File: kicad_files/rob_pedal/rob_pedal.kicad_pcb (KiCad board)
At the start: 2 copper layers, 52 parts, among them J1 OD_IN, J2 ODR_OUT, J3 9V, J4 SHO_IN, J5 SHO_OUT, Q1 BS170, Q2 BS170, Q3 BS170, Q4 BS170

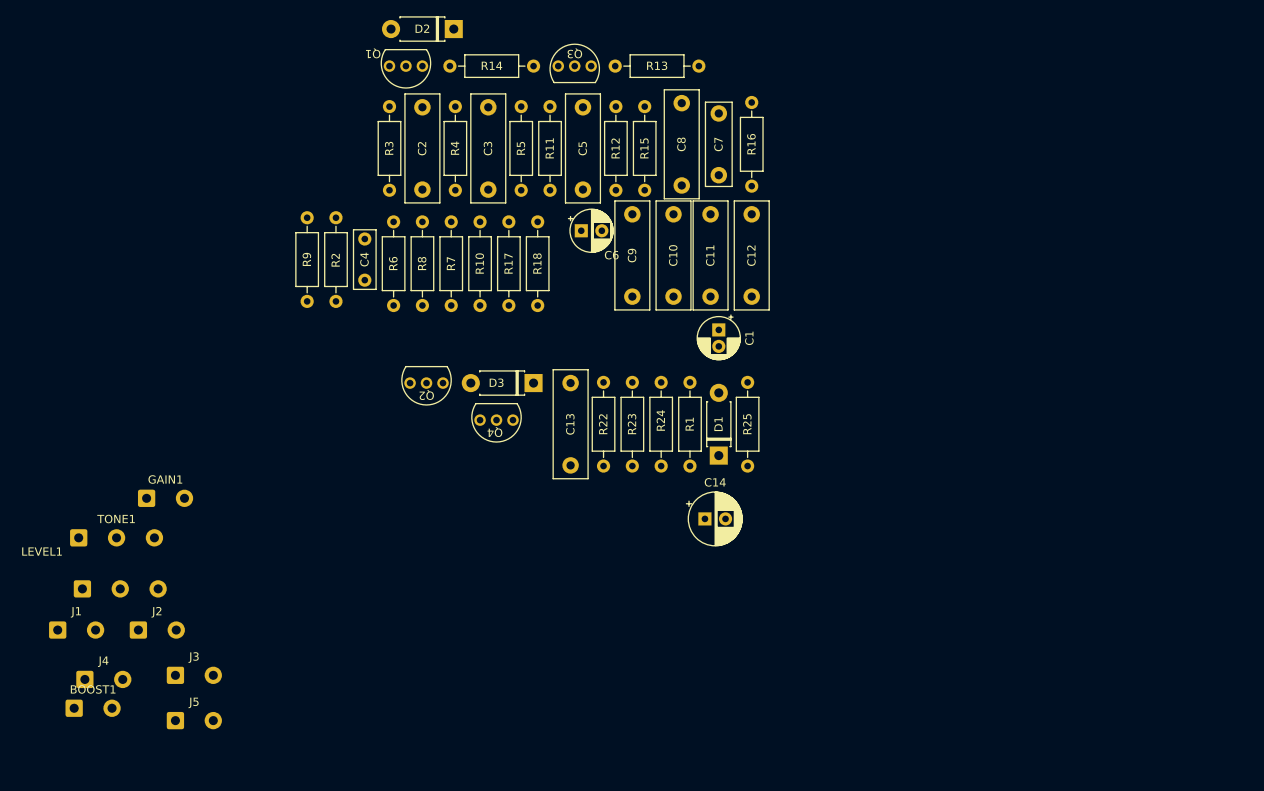
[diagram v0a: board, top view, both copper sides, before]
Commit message: first placement for 125B case
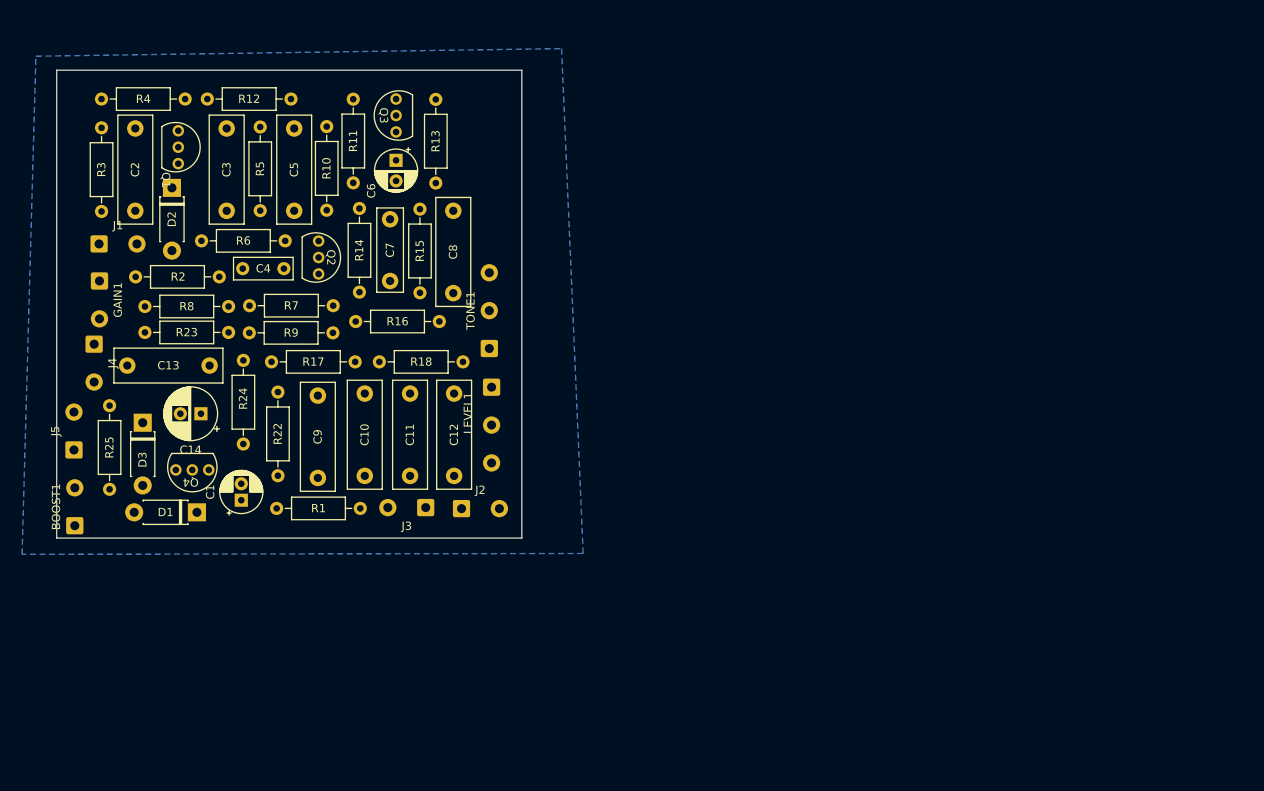
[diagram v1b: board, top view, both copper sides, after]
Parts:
- moved R25 77.8 mm to (52.0, 73.7), turned to -90 degrees
- moved D1 63.8 mm to (62.6, 86.7), turned to 180 degrees
- moved C14 62.5 mm to (63.1, 74.7), turned to 180 degrees
- moved C1 61.6 mm to (68.0, 85.2), turned to 90 degrees
- moved LEVEL1 55.4 mm to (98.4, 71.5), turned to -90 degrees
- moved C13 55.2 mm to (54.1, 68.9), turned to 0 degrees
- moved R16 55.0 mm to (81.9, 63.5), turned to 0 degrees
- moved TONE1 54.9 mm to (98.1, 66.8), turned to 90 degrees
- moved R23 51.7 mm to (66.5, 64.8), turned to 180 degrees
- moved R12 50.8 mm to (63.9, 36.5), turned to 0 degrees
- moved R24 50.8 mm to (68.2, 78.4)
- moved C11 48.4 mm to (88.5, 82.3), turned to 90 degrees
- moved C12 48.1 mm to (93.8, 82.3), turned to 90 degrees
- moved D3 47.7 mm to (56.0, 75.8), turned to -90 degrees
- moved J1 47.2 mm to (50.7, 54.1)
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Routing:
- added copper zone on B.Cu, net GND
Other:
- board outline added: 56.5 x 56.8 mm

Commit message: added routing
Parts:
- moved C1 116.4 mm to (184.3, 79.5), turned to 180 degrees
- moved R8 114.5 mm to (167.8, 87.7), turned to -90 degrees
- moved D1 111.5 mm to (170.5, 115.0), turned to 0 degrees
- moved R7 102.2 mm to (164.5, 97.8), turned to 90 degrees
- moved J5 100.0 mm to (141.0, 115.0), turned to 0 degrees
- moved R14 99.0 mm to (174.8, 85.2), turned to 90 degrees
- moved R18 98.4 mm to (173.3, 111.3), turned to 90 degrees
- moved R25 97.4 mm to (142.4, 110.0), turned to 180 degrees
- moved R9 97.0 mm to (154.0, 111.6), turned to 90 degrees
- moved C7 96.1 mm to (174.5, 88.8)
- moved R15 96.0 mm to (178.0, 87.4)
- moved C8 95.9 mm to (182.0, 97.5)
- moved R16 95.5 mm to (171.0, 97.8), turned to 90 degrees
- moved R24 95.0 mm to (157.3, 111.6)
- moved R17 94.8 mm to (160.5, 101.4), turned to -90 degrees
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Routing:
- net VCC: track 0.00 -> 134.8 mm
- net Net-(C14-Pad1): track 0.00 -> 32.3 mm
- net Net-(D2-Pad2): track 0.00 -> 29.8 mm
- net Net-(R17-Pad1): track 0.00 -> 29.4 mm
- net Net-(BOOST1-Pad1): track 0.00 -> 27.6 mm
- net Net-(C13-Pad2): track 0.00 -> 25.8 mm
- net ODR_IN: track 0.00 -> 21.3 mm
- net Net-(C2-Pad2): track 0.00 -> 20.8 mm
- net Net-(C7-Pad2): track 0.00 -> 19.4 mm
- net Net-(C6-Pad1): track 0.00 -> 19.1 mm
- net Net-(C4-Pad2): track 0.00 -> 18.8 mm
- net IN3: track 0.00 -> 16.3 mm
- net 9V: track 0.00 -> 13.3 mm
- net Net-(C3-Pad1): track 0.00 -> 13.3 mm
- net Net-(C11-Pad2): track 0.00 -> 13.2 mm
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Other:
- board size 56.5 x 56.8 mm -> 63.5 x 46.8 mm

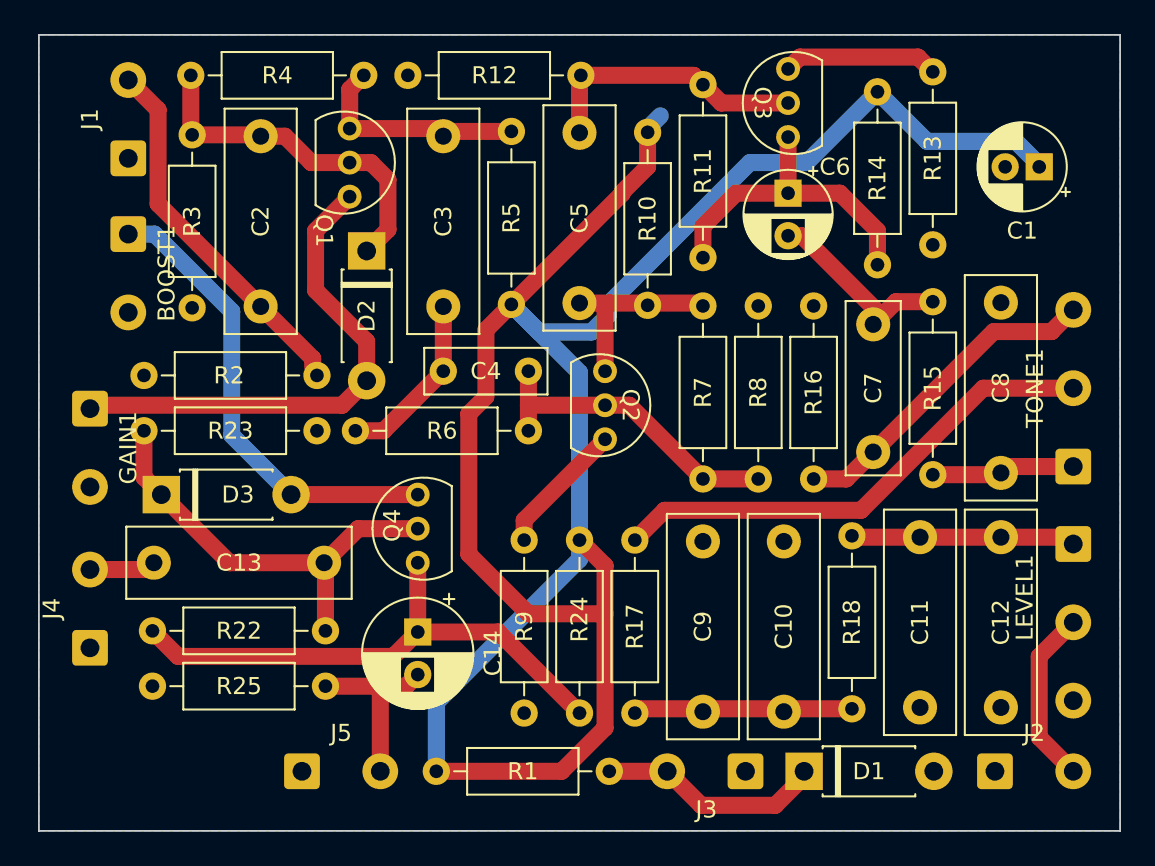
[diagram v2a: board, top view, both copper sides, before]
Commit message: added mounting holes
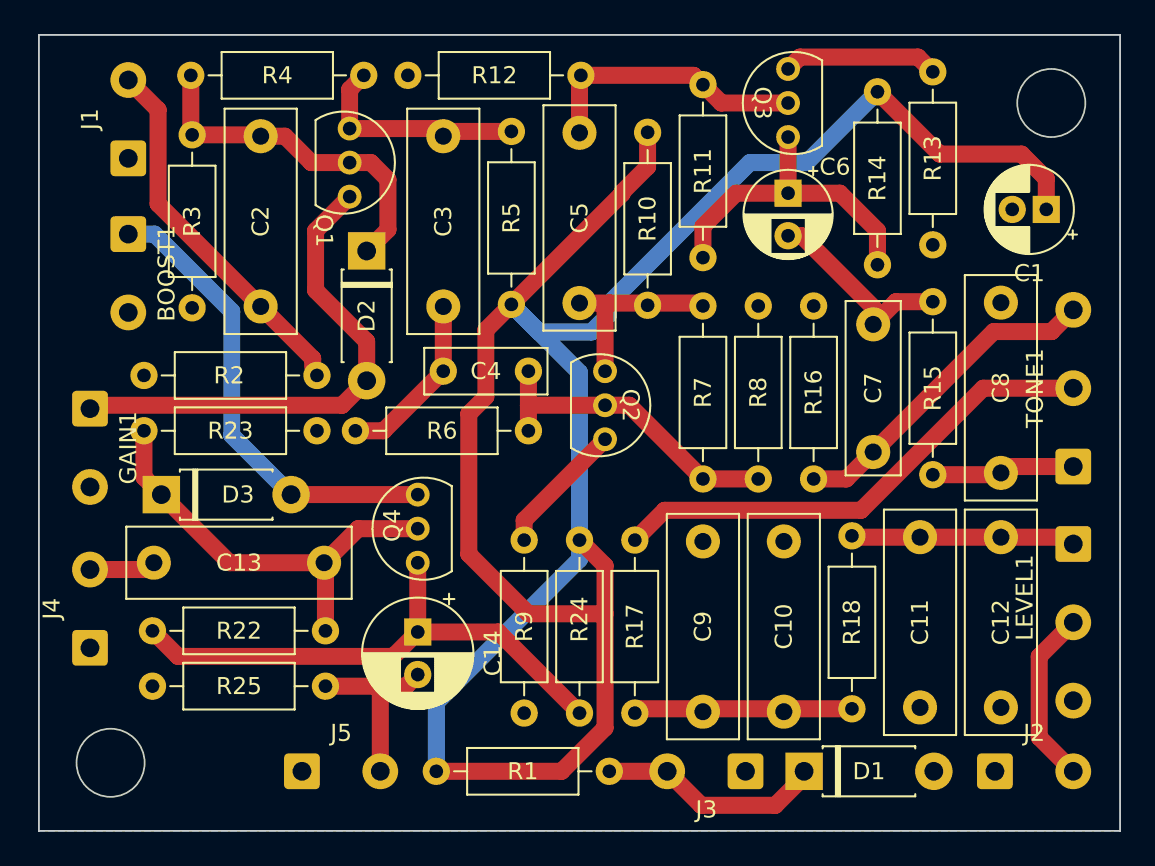
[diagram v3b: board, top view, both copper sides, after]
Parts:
- moved C1 2.53 mm to (184.7, 82.0)
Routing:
- net VCC: track 134.8 -> 136.2 mm
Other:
- outline, holes or cut-outs redrawn
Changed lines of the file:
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@@
   )
   (footprint "Capacitor_THT:CP_Radial_D5.0mm_P2.00mm" (layer "F.Cu")
-    (at 184.29 79.5 180)
+    (at 184.705113 82 180)
     (descr "CP, Radial series, Radial, pin pitch=2.00mm, , diameter=5mm, Electrolytic Capacitor")
     (tags "CP Radial series Radial pin pitch 2.00mm  diameter 5mm Electrolytic Capacitor")
@@
       (net 21 "Net-(D2-Pad2)") (pinfunction "S") (pintype "passive"))
   )
+  (gr_circle (center 129.75 114.5) (end 131.75 114.5) (layer "Edge.Cuts") (width 0.1) (fill none))
   (gr_rect (start 125.54 71.75) (end 189.04 118.5) (layer "Edge.Cuts") (width 0.1) (fill none))
+  (gr_circle (center 185 75.75) (end 187 75.75) (layer "Edge.Cuts") (width 0.1) (fill none))
   (gr_circle (center 123.75 54.496095) (end 131.75 54.246095) (layer "User.1") (width 0.15) (fill none))
   (gr_rect (start 110 39.25) (end 204 158.25) (layer "User.1") (width 0.15) (fill none))
@@
   (segment (start 156.241608 115) (end 158.79 112.451608) (width 1) (layer "F.Cu") (net 3))
   (segment (start 154.29 105.75) (end 150.79 102.25) (width 1) (layer "F.Cu") (net 3))
+  (segment (start 178.45 78.75) (end 183.255113 78.75) (width 1) (layer "F.Cu") (net 3))
   (segment (start 158.79 102.92) (end 157.29 101.42) (width 1) (layer "F.Cu") (net 3))
   (segment (start 159.79 81.08) (end 159.79 81) (width 1) (layer "F.Cu") (net 3))
+  (segment (start 174.79 75.09) (end 178.45 78.75) (width 1) (layer "F.Cu") (net 3))
+  (segment (start 184.705113 80.2) (end 184.705113 82) (width 1) (layer "F.Cu") (net 3))
   (segment (start 159.79 81) (end 161.29 79.5) (width 1) (layer "F.Cu") (net 3))
   (segment (start 150.79 94) (end 151.79 93) (width 1) (layer "F.Cu") (net 3))
@@
   (segment (start 161.29 79.5) (end 161.29 77.47) (width 1) (layer "F.Cu") (net 3))
   (segment (start 148.88 115) (end 156.241608 115) (width 1) (layer "F.Cu") (net 3))
+  (segment (start 183.255113 78.75) (end 184.705113 80.2) (width 1) (layer "F.Cu") (net 3))
   (segment (start 157.29 101.42) (end 157.29 91.58) (width 1) (layer "B.Cu") (net 3))
   (segment (start 153.29 87.58) (end 154.909511 89.199511) (width 1) (layer "B.Cu") (net 3))
   (segment (start 161.29 77.47) (end 161.29 77.25) (width 1) (layer "B.Cu") (net 3))
   (segment (start 157.29 102.55137) (end 148.88 110.96137) (width 1) (layer "B.Cu") (net 3))
-  (segment (start 184.29 79.37937) (end 182.911119 78.000489) (width 1) (layer "B.Cu") (net 3))
   (segment (start 157.29 101.42) (end 157.29 102.55137) (width 1) (layer "B.Cu") (net 3))
   (segment (start 158.989511 87.550489) (end 167.29 79.25) (width 1) (layer "B.Cu") (net 3))
-  (segment (start 182.911119 78.000489) (end 177.700489 78.000489) (width 1) (layer "B.Cu") (net 3))
   (segment (start 157.993962 89.199511) (end 158.989511 88.203962) (width 1) (layer "B.Cu") (net 3))
   (segment (start 158.989511 88.203962) (end 158.989511 87.550489) (width 1) (layer "B.Cu") (net 3))
   (segment (start 170.63 79.25) (end 174.79 75.09) (width 1) (layer "B.Cu") (net 3))
-  (segment (start 184.29 79.5) (end 184.29 79.37937) (width 1) (layer "B.Cu") (net 3))
   (segment (start 148.88 110.96137) (end 148.88 115) (width 1) (layer "B.Cu") (net 3))
-  (segment (start 161.29 77.25) (end 162.04 76.5) (width 1) (layer "B.Cu") (net 3))
   (segment (start 154.909511 89.199511) (end 157.993962 89.199511) (width 1) (layer "B.Cu") (net 3))
-  (segment (start 177.700489 78.000489) (end 174.79 75.09) (width 1) (layer "B.Cu") (net 3))
   (segment (start 167.29 79.25) (end 170.63 79.25) (width 1) (layer "B.Cu") (net 3))
   (segment (start 157.29 91.58) (end 153.29 87.58) (width 1) (layer "B.Cu") (net 3))

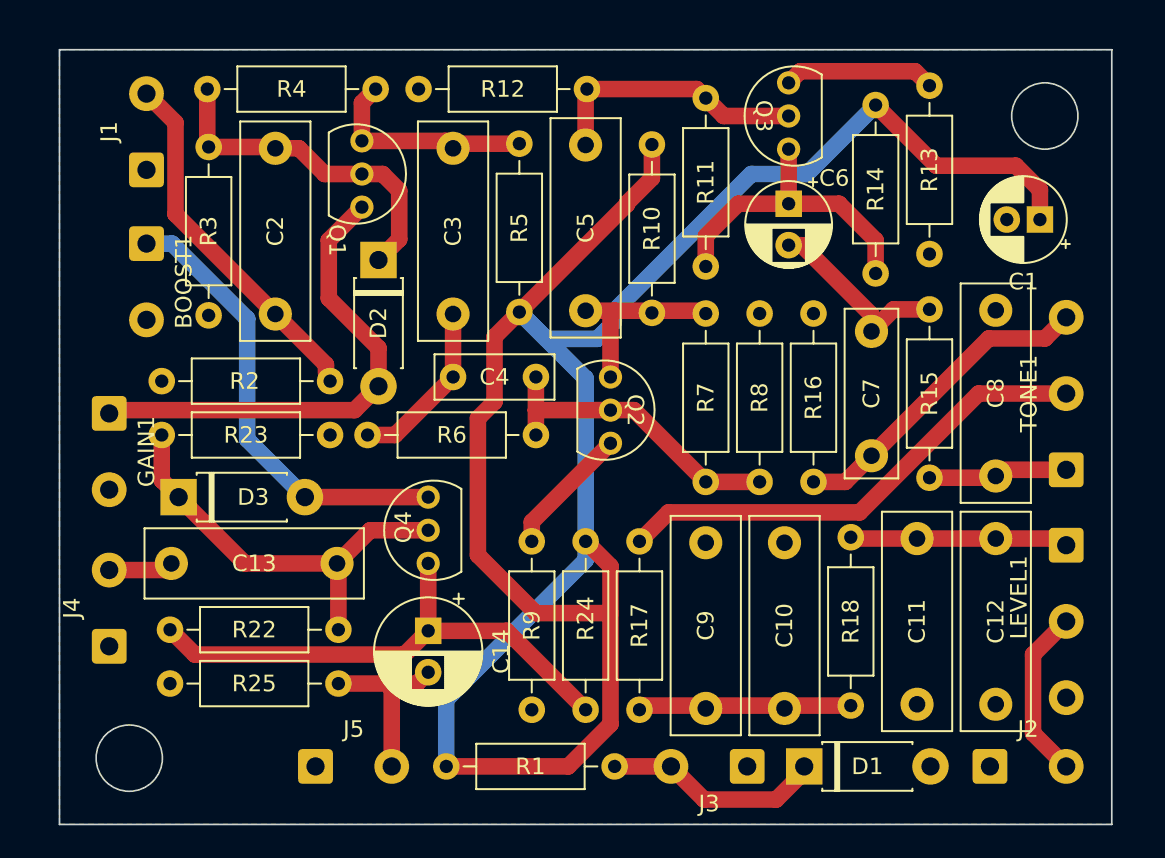
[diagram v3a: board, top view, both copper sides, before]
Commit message: added silkscreen and logo
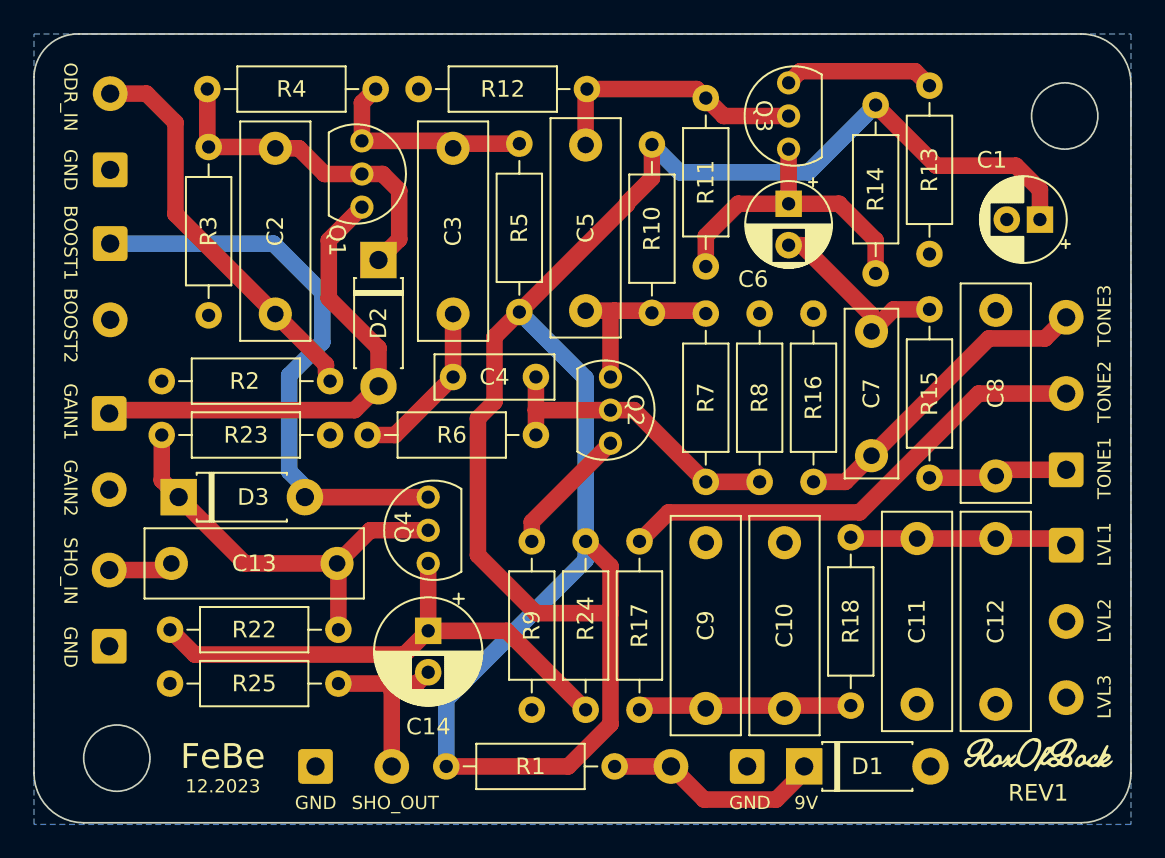
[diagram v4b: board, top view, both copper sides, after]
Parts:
- removed J2: ODR_OUT, Connector_Wire:SolderWire-0.5sqmm_1x02_P4.6mm_D0.9mm_OD2.1mm
- added REV1: logo, footprints:logo, F.Cu at (184.6, 119.3)
- moved BOOST1 2.19 mm to (128.6, 83.5)
- moved J1 2.19 mm to (128.6, 79.0)
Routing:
- net VCC: track 136.2 -> 123.7 mm
- net ODR_OUT: track 10.4 -> 0.00 mm
- net Net-(BOOST1-Pad1): track 27.6 -> 35.0 mm
- net ODR_IN: track 21.3 -> 23.5 mm
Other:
- board size 63.5 x 46.8 mm -> 66.2 x 47.6 mm
- board text added: "12.2023"
- board text added: "9V"
- board text added: "BOOST1"
- board text added: "BOOST2"
- board text added: "FeBe"
- board text added: "GAIN1"
- board text added: "GAIN2"
- board text added: "GND"
- board text added: "LVL1"
- board text added: "LVL2"
- board text added: "LVL3"
- board text added: "ODR_IN"
- board text added: "SHO_IN"
- board text added: "SHO_OUT"
- board text added: "TONE1"
- board text added: "TONE2"
- board text added: "TONE3"
